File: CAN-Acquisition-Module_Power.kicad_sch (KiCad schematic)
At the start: 39 parts, among them J1 Conn_01x04, J2 Conn_01x02, Q1 SI2318A, U1 AZ431LAN, U2 S-8581AA

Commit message: BOM updated for LCSC. Still a WIP.
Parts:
- L1: LCSC (none) -> C96995
- Q1: Do Not Place (none) -> DNP; LCSC (none) -> DNP
- R1: Tolerance (none) -> 5%
- R2: LCSC (none) -> C55912; Tolerance (none) -> 0.1%
- R3, R9: LCSC (none) -> C60590; Tolerance (none) -> 0.1%
- R4: LCSC (none) -> DNP
- R5, R6, R7, R8: Tolerance (none) -> 1%
- U1: LCSC (none) -> C460576
- U2: LCSC (none) -> C3190966
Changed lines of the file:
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@@
+      (effects (font (size 1.27 1.27)) hide)
+    )
+    (property "LCSC" "C460576" (id 6) (at 67.31 170.18 0)
       (effects (font (size 1.27 1.27)) hide)
     )
@@
       (effects (font (size 1.27 1.27)) hide)
     )
+    (property "LCSC" "C55912" (id 6) (at 57.15 166.37 0)
+      (effects (font (size 1.27 1.27)) hide)
+    )
+    (property "Tolerance" "0.1%" (id 7) (at 57.15 166.37 0)
+      (effects (font (size 1.27 1.27)) hide)
+    )
     (pin "1")
     (pin "2")
@@
     )
     (property "P/N" "RN73R1JTTD1502B25" (id 5) (at 57.15 173.99 0)
+      (effects (font (size 1.27 1.27)) hide)
+    )
+    (property "LCSC" "C60590" (id 6) (at 57.15 173.99 0)
+      (effects (font (size 1.27 1.27)) hide)
+    )
+    (property "Tolerance" "0.1%" (id 7) (at 57.15 173.99 0)
       (effects (font (size 1.27 1.27)) hide)
     )
@@
       (effects (font (size 1.27 1.27)) hide)
     )
+    (property "Tolerance" "5%" (id 6) (at 49.53 161.29 0)
+      (effects (font (size 1.27 1.27)) hide)
+    )
     (pin "1")
     (pin "2")
@@
       (effects (font (size 1.27 1.27)) hide)
     )
+    (property "LCSC" "C96995" (id 6) (at 39.37 161.29 0)
+      (effects (font (size 1.27 1.27)) hide)
+    )
     (pin "1")
     (pin "2")
@@
     )
     (property "Do Not Place" "DNP" (id 4) (at 162.56 29.21 0))
+    (property "LCSC" "DNP" (id 5) (at 158.75 25.4 0)
+      (effects (font (size 1.27 1.27)) hide)
+    )
     (pin "1")
     (pin "2")
@@
     )
     (property "P/N" "S-8581AA-A8T1U7" (id 5) (at 187.96 92.71 0)
+      (effects (font (size 1.27 1.27)) hide)
+    )
+    (property "LCSC" "C3190966" (id 6) (at 187.96 92.71 0)
       (effects (font (size 1.27 1.27)) hide)
     )
@@
       (effects (font (size 1.27 1.27)) hide)
     )
+    (property "Tolerance" "1%" (id 6) (at 173.99 44.45 0)
+      (effects (font (size 1.27 1.27)) hide)
+    )
     (pin "1")
     (pin "2")
@@
       (effects (font (size 1.27 1.27)) hide)
     )
+    (property "Tolerance" "1%" (id 6) (at 227.33 53.34 0)
+      (effects (font (size 1.27 1.27)) hide)
+    )
     (pin "1")
     (pin "2")
@@
     )
     (property "P/N" "RN73R1JTTD1502B25" (id 5) (at 232.41 105.41 0)
+      (effects (font (size 1.27 1.27)) hide)
+    )
+    (property "LCSC" "C60590" (id 6) (at 232.41 105.41 0)
+      (effects (font (size 1.27 1.27)) hide)
+    )
+    (property "Tolerance" "0.1%" (id 7) (at 232.41 105.41 0)
       (effects (font (size 1.27 1.27)) hide)
     )
@@
       (effects (font (size 1.27 1.27)) hide)
     )
+    (property "Tolerance" "1%" (id 6) (at 180.34 46.99 0)
+      (effects (font (size 1.27 1.27)) hide)
+    )
     (pin "1")
     (pin "2")
@@
       (effects (font (size 1.27 1.27)) hide)
     )
+    (property "Do Not Place" "DNP" (id 7) (at 236.22 53.34 0)
+      (effects (font (size 1.27 1.27)) hide)
+    )
+    (property "LCSC" "DNP" (id 8) (at 236.22 53.34 0)
+      (effects (font (size 1.27 1.27)) hide)
+    )
     (pin "1")
     (pin "2")
@@
       (effects (font (size 1.27 1.27)) hide)
     )
+    (property "Tolerance" "1%" (id 6) (at 232.41 99.06 0)
+      (effects (font (size 1.27 1.27)) hide)
+    )

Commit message: BOM updated for LCSC. Still a WIP
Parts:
- D1, D2, D6: LCSC (none) -> C2762696
- D3: LCSC (none) -> C284078
- D4, D5: LCSC (none) -> C558429
- F1: Alternate P/N (none) -> nSMD010; LCSC (none) -> C70065
- J1, J2, NT1: Do Not Place (none) -> DNP; LCSC (none) -> DNP
- L2: LCSC (none) -> C703770
- L3: Alternate P/N (none) -> MLP2520S4R7MT0S1; LCSC (none) -> C91237
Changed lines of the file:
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@@
+      (effects (font (size 1.27 1.27)) hide)
+    )
+    (property "Do Not Place" "DNP" (id 4) (at 264.16 35.56 0)
+      (effects (font (size 1.27 1.27)) hide)
+    )
+    (property "LCSC" "DNP" (id 5) (at 264.16 35.56 0)
       (effects (font (size 1.27 1.27)) hide)
     )
@@
       (effects (font (size 1.27 1.27)) hide)
     )
+    (property "LCSC" "C2762696" (id 6) (at 238.76 34.29 0)
+      (effects (font (size 1.27 1.27)) hide)
+    )
     (pin "1")
     (pin "2")
@@
     )
     (property "P/N" "CPDT-24V" (id 5) (at 91.44 102.87 0)
+      (effects (font (size 1.27 1.27)) hide)
+    )
+    (property "LCSC" "C284078" (id 6) (at 91.44 102.87 0)
       (effects (font (size 1.27 1.27)) hide)
     )
@@
       (effects (font (size 1.27 1.27)) hide)
     )
+    (property "LCSC" "C703770" (id 6) (at 124.46 95.25 0)
+      (effects (font (size 1.27 1.27)) hide)
+    )
     (pin "1")
     (pin "2")
@@
       (effects (font (size 1.27 1.27)) hide)
     )
+    (property "Do Not Place" "DNP" (id 4) (at 189.23 49.53 0)
+      (effects (font (size 1.27 1.27)) hide)
+    )
+    (property "LCSC" "DNP" (id 5) (at 189.23 49.53 0)
+      (effects (font (size 1.27 1.27)) hide)
+    )
     (pin "1")
     (pin "2")
@@
     )
     (property "P/N" "D1213A-01SO-7" (id 5) (at 168.91 26.67 0)
+      (effects (font (size 1.27 1.27)) hide)
+    )
+    (property "LCSC" "C558429" (id 6) (at 168.91 26.67 0)
       (effects (font (size 1.27 1.27)) hide)
     )
@@
       (effects (font (size 1.27 1.27)) hide)
     )
+    (property "LCSC" "C2762696" (id 6) (at 135.89 83.82 0)
+      (effects (font (size 1.27 1.27)) hide)
+    )
     (pin "1")
     (pin "2")
@@
     )
     (property "P/N" "D1213A-01SO-7" (id 5) (at 146.05 26.67 0)
+      (effects (font (size 1.27 1.27)) hide)
+    )
+    (property "LCSC" "C558429" (id 6) (at 146.05 26.67 0)
       (effects (font (size 1.27 1.27)) hide)
     )
@@
     )
     (property "P/N" "CUS05S40,H3F" (id 5) (at 74.93 95.25 0)
+      (effects (font (size 1.27 1.27)) hide)
+    )
+    (property "LCSC" "C2762696" (id 6) (at 74.93 95.25 0)
       (effects (font (size 1.27 1.27)) hide)
     )
@@
       (effects (font (size 1.27 1.27)) hide)
     )
+    (property "Alternate P/N" "nSMD010" (id 6) (at 62.23 95.25 0)
+      (effects (font (size 1.27 1.27)) hide)
+    )
+    (property "LCSC" "C70065" (id 7) (at 62.23 95.25 0)
+      (effects (font (size 1.27 1.27)) hide)
+    )
     (pin "1")
     (pin "2")
@@
       (effects (font (size 1.27 1.27)) hide)
     )
+    (property "Alternate P/N" "MLP2520S4R7MT0S1" (id 6) (at 214.63 95.25 0)
+      (effects (font (size 1.27 1.27)) hide)
+    )
+    (property "LCSC" "C91237" (id 7) (at 214.63 95.25 0)
+      (effects (font (size 1.27 1.27)) hide)
+    )
     (pin "1")
     (pin "2")
@@
       (effects (font (size 1.27 1.27)) hide)
     )
+    (property "Do Not Place" "DNP" (id 4) (at 151.13 95.25 0)
+      (effects (font (size 1.27 1.27)) hide)
+    )
+    (property "LCSC" "DNP" (id 5) (at 151.13 95.25 0)
+      (effects (font (size 1.27 1.27)) hide)
+    )

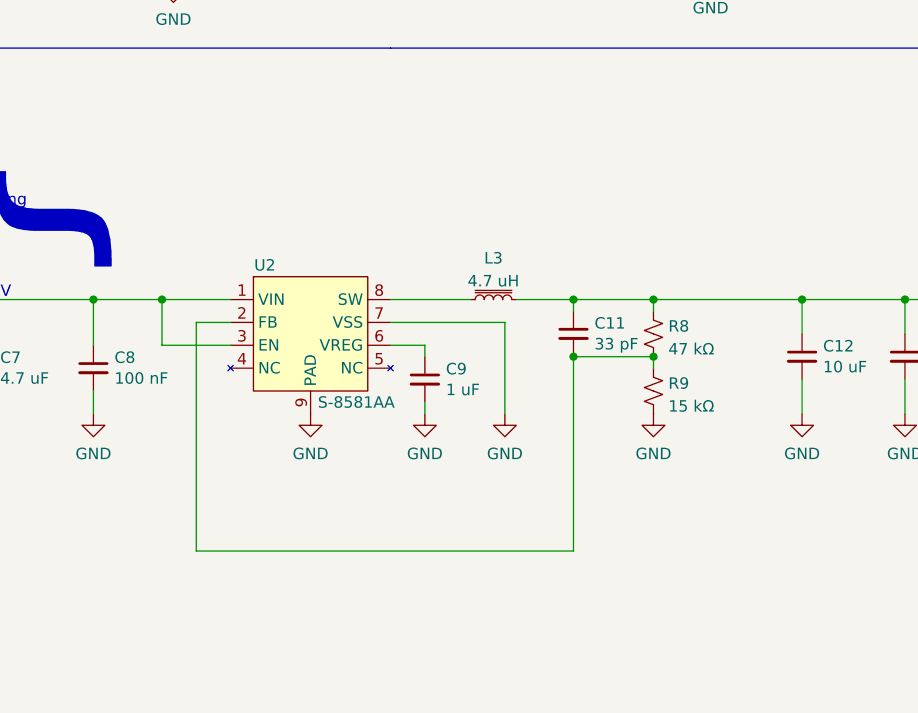
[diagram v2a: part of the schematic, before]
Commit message: Created Rev B1
Replaced buck regulator S-8581AA with AP63200 because of shortage
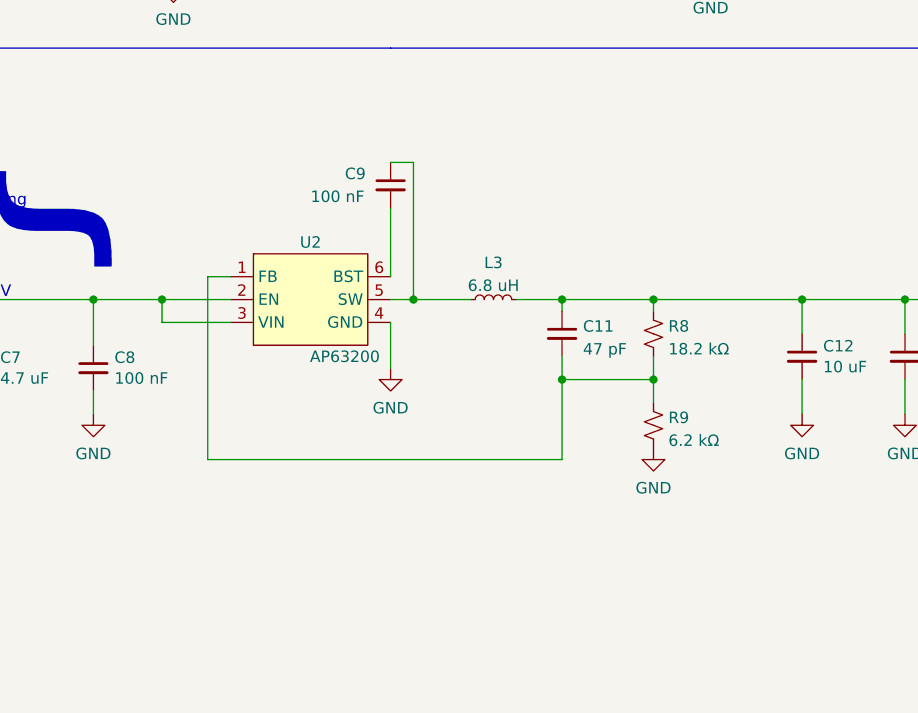
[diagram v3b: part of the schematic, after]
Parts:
- removed L3: 4.7 uH, Inductor_SMD:L_1008_2520Metric, symbol Device:L_Iron_Small
- removed U2: S-8581AA, CAN-Acquisition-Module:Ablic_HSTN-8-A, symbol CAN-Acquisition-Module:S-8581AA
- added L3: 6.8 uH, CAN-Acquisition-Module:Murata_LQH3_1212(3030_Metric), symbol Device:L_Small
- added U2: AP63200, CAN-Acquisition-Module:Diodes-Inc_TSOT26, symbol CAN-Acquisition-Module:AP63200
- C1, C12, C13, C2: LCSC P/N (none) -> C386019; LCSC Package (none) -> 0805; LCSC Specs (none) -> 10uF X7R 6.3V
- C10, C3, C4, C7: LCSC P/N (none) -> C92853; LCSC Package (none) -> 1206; LCSC Specs (none) -> 4.7uF X7R 50V
- C11: value 33 pF -> 47 pF; LCSC P/N (none) -> C126580; LCSC Package (none) -> 0603; LCSC Specs (none) -> 47pF NP0/C0G 50V; Mfr. Kemet -> Samsung; P/N C0603C330J1GACAUTO -> CL10C470JB81PNC
- C14: LCSC P/N (none) -> C77014; LCSC Package (none) -> 0402; LCSC Specs (none) -> 100nF X7R 16V
- C5, C8: LCSC P/N (none) -> C314282; LCSC Package (none) -> 0603; LCSC Specs (none) -> 100nF X7R 50V
- C6: LCSC P/N (none) -> DNP; LCSC Package (none) -> DNP; LCSC Specs (none) -> DNP
- C9: value 1 uF -> 100 nF; LCSC P/N (none) -> C314282; LCSC Package (none) -> 0603; LCSC Specs (none) -> 100nF X7R 50V; Mfr. Samsung Electro-Mechanics -> Samsung Electro-Mechanics; P/N CL10B105KA8NNNC -> CL10B104KB8NNWC; Rated Voltage 25V -> 50V
- D1, D2, D6: LCSC C2762696 -> (none); LCSC P/N (none) -> C2762696; LCSC Package (none) -> USC; LCSC Specs (none) -> CUS05S40.H3F
- D3: LCSC C284078 -> (none); LCSC P/N (none) -> C284078; LCSC Package (none) -> SOT-23; LCSC Specs (none) -> PESD2CAN
- D4, D5: LCSC C558429 -> (none); LCSC P/N (none) -> C558429; LCSC Package (none) -> SOT-23; LCSC Specs (none) -> TPCM1213A-01SO
- F1: Alternate P/N nSMD010 -> (none); LCSC C70065 -> (none); LCSC P/N (none) -> C70065; LCSC Package (none) -> 1206; LCSC Specs (none) -> nSMD010
- J1, J2, NT1, R4: LCSC DNP -> (none); LCSC P/N (none) -> DNP; LCSC Package (none) -> DNP; LCSC Specs (none) -> DNP
- L1: LCSC C96995 -> (none); LCSC P/N (none) -> C96995; LCSC Package (none) -> 0603; LCSC Specs (none) -> UPZ1608E101-3R0TF
- L2: LCSC C703770 -> (none); LCSC P/N (none) -> C394141; LCSC Package (none) -> 1812; LCSC Specs (none) -> FHW1812IF471KST
- Q1: Alternate P/N IRLML0040 -> (none); LCSC DNP -> (none); LCSC P/N (none) -> DNP; LCSC Package (none) -> DNP; LCSC Specs (none) -> DNP
- R1: LCSC P/N (none) -> C17408; LCSC Package (none) -> 0805; LCSC Specs (none) -> 100R 5%
- R2: LCSC C55912 -> (none); LCSC P/N (none) -> C55912; LCSC Package (none) -> 0603; LCSC Specs (none) -> 6K8 0.1%
- R3: LCSC C60590 -> (none); LCSC P/N (none) -> C60590; LCSC Package (none) -> 0603; LCSC Specs (none) -> 15K 0.1%
- R5, R6, R7: LCSC P/N (none) -> C98220; LCSC Package (none) -> 0603; LCSC Specs (none) -> 10K 1%
- R8: value 47 kΩ -> 18.2 kΩ; LCSC P/N (none) -> C22892; LCSC Package (none) -> 0603; LCSC Specs (none) -> 18K2 1%; Mfr. TE Connectivity -> (none); P/N CRGCQ0603F47K -> (none)
- R9: value 15 kΩ -> 6.2 kΩ; footprint Resistor_SMD:R_0603_1608Metric -> Resistor_SMD:R_0805_2012Metric; LCSC C60590 -> (none); LCSC P/N (none) -> C351551; LCSC Package (none) -> 0805; LCSC Specs (none) -> 6K2 0.1%; Mfr. KOA Speer -> Panasonic; P/N RN73R1JTTD1502B25 -> ERA-6AEB622V
- U1: LCSC C460576 -> (none); LCSC P/N (none) -> C460576; LCSC Package (none) -> SOT-23; LCSC Specs (none) -> AZ431LANTR
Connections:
- net +3V3: now also L3.2
- net GND: now also U2.4 (GND); no longer C9.2
- net at C7.1, C8.1, NT1.2: now also U2.2 (EN), U2.3 (VIN)
- net at C11.2, R8.2, R9.1: now also U2.1 (FB)
- net at C9.1: now also L3.1, U2.5 (SW)
- new net: C9.2, U2.6 (BST)
